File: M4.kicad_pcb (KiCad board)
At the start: 2 copper layers, 57.5 x 105 mm, 181 parts, among them J1 PJ-301B, J10 PJ-301B, J11 PJ-301B, J12 PJ-301B, J13 PJ-301B, J2 PJ-301B, J3 PJ-301B, J4 PJ-301B, J5 PJ-301B, J6 PJ-301B, J7 PJ-301B, J8 PJ-301B, J9 PJ-301B, P1 CONN_01X01, P2 CONN_01X01, P3 CONN_01X01, P4 CONN_01X01, P5 CONN_01X06, P6 CONN_02X05, P7 CONN_01X01, SW1 B3F-1050, SW2 B3F-1050, SW3 B3F-1050, SW4 B3F-1050, SW5 B3F-1050, SW6 B3F-1050, SW7 B3F-1050, U1 LM1117, U10 STM32F410RBTx, U2 MCP1703, U3 MAX5134, U4 74ACT541, U5 OPA4171, U6 OPA171, U7 OPA171, U8 CD4051, U9 OPA4171, X1 MIDI IN, Y1 8MHz

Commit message: routing.
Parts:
- C1, C10, C11, C33, C34, C4, C43, C44, C5, C6, C7, C8, C9, D24, D25, L1, L3, L4, P5, P6, R10, R11, R12, R13, R14, R15, R17, R18, R2, R20, R21, R8, R9, U6: moved to B.Cu
- Y1: footprint synth:HC-49-SM -> synth:403-XTAL-4-SMD
- moved L4 170.2 mm to (161.1, 55.0)
- moved L3 165.9 mm to (161.1, 39.5)
- moved D25 164.2 mm to (155.7, 52.1), turned to 270 degrees
- moved R14 162.3 mm to (134.2, 91.2), turned to 90 degrees
- moved C9 161.8 mm to (135.5, 88.5), turned to 180 degrees
- moved D24 161.3 mm to (155.7, 42.2), turned to 270 degrees
- moved U6 159.8 mm to (127.6, 96.2), turned to 270 degrees
- moved C33 158.3 mm to (134.5, 83.4)
- moved R8 157.6 mm to (131.4, 87.1), turned to 270 degrees
- moved R13 157.3 mm to (127.7, 91.9)
- moved R12 156.3 mm to (127.7, 90.1), turned to 180 degrees
- moved R17 156.2 mm to (136.0, 76.9)
- moved R9 156.1 mm to (129.6, 87.1), turned to 270 degrees
- moved R18 153.6 mm to (133.0, 76.9), turned to 180 degrees
- moved C8 152.6 mm to (130.6, 78.9), turned to 180 degrees
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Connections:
- U3 pad 11: Net-(U3-Pad11) -> /DAC_CH2
- U3 pad 14: Net-(U3-Pad14) -> /DAC_CH1
- U3 pad 3: Net-(U3-Pad3) -> /DAC_CH0
- U3 pad 6: Net-(U3-Pad6) -> /DAC_CH3
- U5 pad 10: Net-(U3-Pad11) -> /DAC_CH1
- U5 pad 12: Net-(U3-Pad6) -> /DAC_CH2
- U5 pad 3: Net-(U3-Pad3) -> /DAC_CH3
- U5 pad 5: Net-(U3-Pad14) -> /DAC_CH0
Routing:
- net Net-(C4-Pad1): track 0.00 -> 32.2 mm
- net /VREF: track 0.00 -> 26.8 mm
- net Net-(C8-Pad2): track 0.00 -> 21.7 mm
- net /DAC_CH1: track 0.00 -> 17.8 mm
- net /DAC_CH0: track 0.00 -> 17.7 mm
- net +3V3: track 0.00 -> 16.3 mm
- net /DAC_CH2: track 0.00 -> 14.2 mm
- net /DAC_CH3: track 0.00 -> 14.1 mm
- net Net-(C11-Pad2): track 0.00 -> 13.0 mm
- net /DAC_AVDD: track 0.00 -> 7.03 mm
- net Net-(R12-Pad1): track 0.00 -> 5.00 mm
- net +12V: track 0.00 -> 4.51 mm, vias 0 -> 2
- net Net-(C8-Pad1): track 0.00 -> 4.43 mm
- net Net-(C10-Pad2): track 0.00 -> 4.40 mm
- net -12V: track 0.00 -> 4.25 mm, vias 0 -> 2
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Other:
- board size 57.5 x 105 mm -> 57.2 x 105 mm
- net class Default: via_dia 0.6 -> 0.8
- net class POWER added: clearance 0.2, trace_width 0.4, via_dia 0.9, via_drill 0.45

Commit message: routing..
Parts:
- L2, P1, P2, R16, R22, R23, R24, R25, R26, R27, R28, R29, U7: moved to B.Cu
- moved U7 178.7 mm to (142.8, 116.8), turned to 270 degrees
- moved C12 159.1 mm to (110.0, 115.0)
- moved C13 159.1 mm to (110.0, 115.0)
- moved C16 159.1 mm to (110.0, 115.0)
- moved C17 159.1 mm to (110.0, 115.0)
- moved C18 159.1 mm to (110.0, 115.0)
- moved C19 159.1 mm to (110.0, 115.0)
- moved C20 159.1 mm to (110.0, 115.0)
- moved C21 159.1 mm to (110.0, 115.0)
- moved C22 159.1 mm to (110.0, 115.0)
- moved C23 159.1 mm to (110.0, 115.0)
- moved C24 159.1 mm to (110.0, 115.0)
- moved C25 159.1 mm to (110.0, 115.0)
- moved C26 159.1 mm to (110.0, 115.0)
- moved C27 159.1 mm to (110.0, 115.0)
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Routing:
- net /MIDI_RX: track 0.00 -> 117.6 mm, vias 0 -> 2
- net /12b_DAC: track 0.00 -> 101.9 mm, vias 0 -> 2
- net +3V3: track 16.3 -> 110.5 mm, vias 0 -> 3
- net +12V: track 4.51 -> 59.9 mm, vias 2 -> 3
- net -12V: track 4.25 -> 55.6 mm, vias 2 -> 3
- net Net-(C46-Pad1): track 0.00 -> 43.7 mm, vias 0 -> 1
- net /LED11: track 0.00 -> 33.3 mm, vias 0 -> 1
- net /~DAC_SEL: track 0.00 -> 33.2 mm, vias 0 -> 2
- net /LED3: track 0.00 -> 28.6 mm, vias 0 -> 1
- net /LED10: track 0.00 -> 26.7 mm, vias 0 -> 1
- net /DAC_SCK: track 0.00 -> 26.4 mm, vias 0 -> 2
- net /~LDAC: track 0.00 -> 25.6 mm, vias 0 -> 2
- net /SWCLK: track 0.00 -> 25.4 mm, vias 0 -> 2
- net Net-(C45-Pad1): track 0.00 -> 23.5 mm, vias 0 -> 1
- net /LED2: track 0.00 -> 23.1 mm, vias 0 -> 1
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
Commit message: routing...
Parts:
- C12, C17, C26, C27, C28, C29, C30, C31, C45, D22, P7, R30, R31, R32, R33, R34, R41, R47, R52, R53: moved to B.Cu
- moved P7 73.9 mm to (126.5, 43.0)
- moved C45 71.7 mm to (133.5, 47.3), turned to 180 degrees
- moved C27 70.7 mm to (130.4, 47.3)
- moved C29 68.0 mm to (112.3, 47.0), turned to 180 degrees
- moved C17 66.6 mm to (129.8, 51.4)
- moved R53 65.9 mm to (112.3, 49.1), turned to 180 degrees
- moved C30 65.0 mm to (129.8, 53.1)
- moved C28 63.3 mm to (129.8, 54.9)
- moved R32 60.8 mm to (145.1, 65.4), turned to 180 degrees
- moved R33 60.7 mm to (142.6, 63.8), turned to 90 degrees
- moved C31 56.2 mm to (117.1, 59.2), turned to 270 degrees
- moved C26 56.1 mm to (115.3, 59.2), turned to 270 degrees
- moved R31 55.7 mm to (135.9, 65.7), turned to 180 degrees
- moved R30 52.9 mm to (126.8, 64.8), turned to 90 degrees
- moved R34 48.1 mm to (155.4, 130.8), turned to 90 degrees
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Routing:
- net /MODE_SW: track 0.00 -> 133.0 mm, vias 0 -> 1
- net /CH3_SW: track 0.00 -> 109.4 mm, vias 0 -> 1
- net /MIDI_LED: track 0.00 -> 104.3 mm, vias 0 -> 3
- net /LED12: track 0.00 -> 81.0 mm, vias 0 -> 1
- net /GATE4_LED: track 0.00 -> 71.5 mm, vias 0 -> 2
- net /D1: track 0.00 -> 60.9 mm, vias 0 -> 1
- net /D0: track 0.00 -> 59.9 mm, vias 0 -> 1
- net /GATE_3: track 0.00 -> 59.2 mm, vias 0 -> 1
- net /CLOCK: track 0.00 -> 57.3 mm, vias 0 -> 1
- net /GATE3_LED: track 0.00 -> 57.1 mm, vias 0 -> 2
- net /~MUX_SEL: track 0.00 -> 56.8 mm, vias 0 -> 1
- net /REC_SW: track 9.47 -> 63.5 mm, vias 1 -> 2
- net +3V3: track 110.5 -> 154.5 mm, vias 3 -> 5
- net /GATE2_LED: track 0.00 -> 41.6 mm, vias 0 -> 2
- net /GATE1_LED: track 8.07 -> 29.4 mm, vias 1 -> 2
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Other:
- net class Default: trace_width 0.25 -> 0.2; via_dia 0.8 -> 0.7; via_drill 0.4 -> 0.35

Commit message: routing....
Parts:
- C47, D23, R4, R62, R63: moved to B.Cu
- moved R63 30.5 mm to (137.7, 127.8), turned to 270 degrees
- moved C47 30.3 mm to (133.7, 133.9)
- moved R4 26.4 mm to (135.2, 122.8), turned to 180 degrees
- moved R62 19.2 mm to (120.0, 131.4), turned to 180 degrees
- moved D23 17.4 mm to (120.9, 128.6), turned to 270 degrees
- moved R22 5.61 mm to (138.0, 50.1)
- moved R24 4.53 mm to (138.6, 53.1), turned to 270 degrees
- moved C2 3.91 mm to (113.9, 113.9)
- moved C13 3.91 mm to (113.8, 114.1)
- moved C16 3.91 mm to (113.8, 114.1)
- moved C18 3.91 mm to (113.8, 114.1)
- moved C19 3.91 mm to (113.8, 114.1)
- moved C20 3.91 mm to (113.8, 114.1)
- moved C21 3.91 mm to (113.8, 114.1)
- moved C22 3.91 mm to (113.8, 114.1)
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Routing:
- net /LED13: track 2.83 -> 138.1 mm, vias 1 -> 2
- net /LED15: track 2.97 -> 137.9 mm, vias 1 -> 2
- net /LED14: track 2.79 -> 136.2 mm, vias 1 -> 2
- net /CH4_SW: track 2.24 -> 119.2 mm
- net +3V3: track 154.5 -> 262.6 mm, vias 5 -> 7
- net /CH2_SW: track 2.27 -> 93.6 mm
- net /GATE_2: track 2.04 -> 78.9 mm, vias 1 -> 2
- net /GATE_1: track 2.27 -> 78.1 mm, vias 1 -> 2
- net /CH1_SW: track 2.45 -> 77.8 mm
- net +12V: track 74.1 -> 147.9 mm
- net /GATE_4: track 1.69 -> 70.5 mm, vias 1 -> 2
- net -12V: track 66.9 -> 129.7 mm, vias 4 -> 6
- net +5V: track 0.00 -> 48.3 mm
- net /LED12: track 81.0 -> 127.6 mm, vias 1 -> 2
- net Net-(D23-Pad2): track 0.00 -> 19.8 mm
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
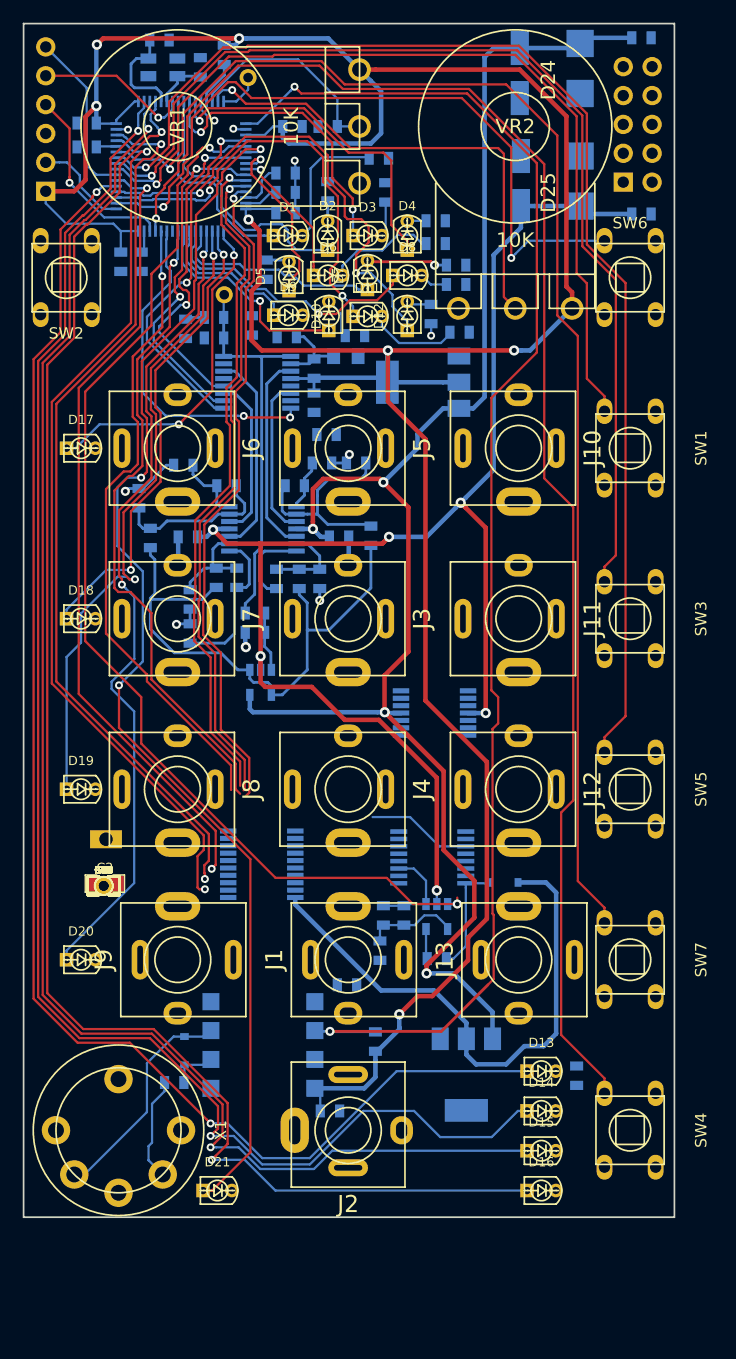
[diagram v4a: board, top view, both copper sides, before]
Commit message: basically routed. need to delete excess decoupling caps and decide about whether external sw pull up resistors are necessary - probably not and need to be deleted
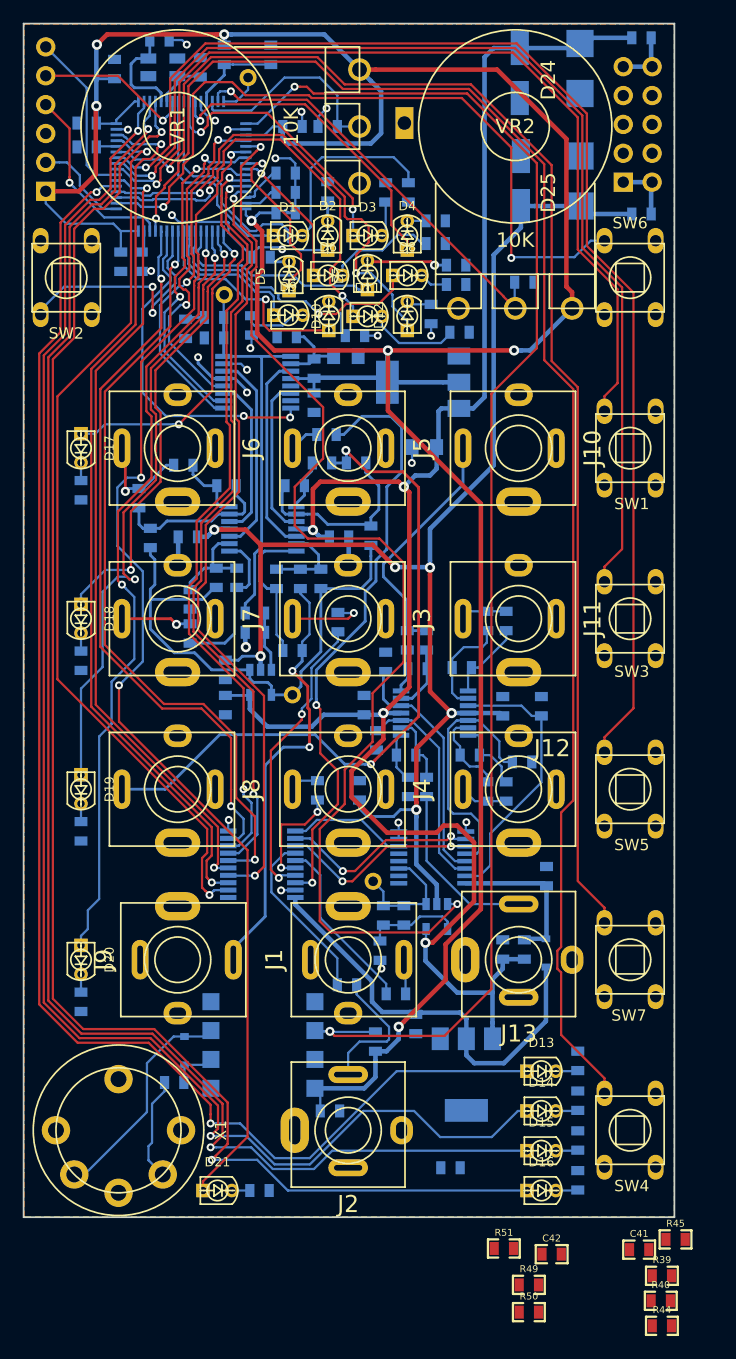
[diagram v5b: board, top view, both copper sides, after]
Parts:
- C13, C16, C18, C19, C2, C20, C21, C22, C23, C24, C25, C3, C32, C35, C36, C37, C38, C39, C40, C46, P3, P4, R1, R19, R3, R35, R36, R37, R38, R42, R43, R46, R48, R5, R54, R55, R56, R57, R58, R59, R6, R60, R61: moved to B.Cu
- moved C32 74.6 mm to (128.5, 41.0), turned to 90 degrees
- moved C16 71.9 mm to (114.8, 42.2), turned to 90 degrees
- moved P1 68.2 mm to (140.2, 47.0), turned to 90 degrees
- moved C46 64.7 mm to (150.8, 61.0)
- moved R44 62.5 mm to (162.9, 152.8)
- moved R40 61.1 mm to (162.8, 150.6)
- moved R39 59.9 mm to (162.9, 148.4)
- moved R45 59.1 mm to (164.1, 145.2)
- moved C41 56.9 mm to (160.9, 146.1)
- moved R50 53.0 mm to (151.2, 151.6)
- moved R49 51.3 mm to (151.2, 149.2)
- moved C42 51.0 mm to (153.2, 146.5)
- moved R37 49.1 mm to (155.5, 140.0), turned to 270 degrees
- moved C2 47.6 mm to (142.0, 75.5), turned to 180 degrees
- moved R51 47.5 mm to (149.0, 146.0)
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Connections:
- R14 pad 1: Net-(J7-Pad3) -> Net-(J9-Pad3)
- R15 pad 1: Net-(J8-Pad3) -> Net-(J7-Pad3)
- R16 pad 1: Net-(J9-Pad3) -> Net-(J6-Pad3)
- R17 pad 1: Net-(J6-Pad3) -> Net-(J8-Pad3)
- R18 pad 1: Net-(J6-Pad3) -> Net-(J8-Pad3)
- R19 pad 1: Net-(J7-Pad3) -> Net-(J9-Pad3)
- R20 pad 1: Net-(J8-Pad3) -> Net-(J7-Pad3)
- R21 pad 1: Net-(J9-Pad3) -> Net-(J6-Pad3)
- R55 pad 1: Net-(J11-Pad3) -> Net-(J13-Pad3)
- R56 pad 1: Net-(J12-Pad3) -> Net-(J11-Pad3)
- R57 pad 1: Net-(J13-Pad3) -> Net-(J12-Pad3)
- R59 pad 1: Net-(J11-Pad3) -> Net-(J13-Pad3)
- R60 pad 1: Net-(J12-Pad3) -> Net-(J11-Pad3)
- R61 pad 1: Net-(J13-Pad3) -> Net-(J12-Pad3)
- U9 pad 1: Net-(C22-Pad1) -> Net-(C23-Pad1)
- U9 pad 2: Net-(C22-Pad2) -> Net-(C23-Pad2)
- U9 pad 3: Net-(C18-Pad1) -> Net-(C19-Pad1)
- U9 pad 5: Net-(C19-Pad1) -> Net-(C18-Pad1)
- U9 pad 6: Net-(C23-Pad2) -> Net-(C22-Pad2)
- U9 pad 7: Net-(C23-Pad1) -> Net-(C22-Pad1)
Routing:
- net Net-(J8-Pad3): track 2.52 -> 61.2 mm, vias 1 -> 2
- net Net-(R7-Pad2): track 0.00 -> 53.2 mm, vias 0 -> 2
- net GND: track 16.5 -> 55.1 mm, vias 6 -> 23
- net Net-(J9-Pad3): track 5.20 -> 38.3 mm, vias 1 -> 2
- net Net-(R5-Pad2): track 0.00 -> 25.9 mm, vias 0 -> 2
- net Net-(C20-Pad1): track 0.00 -> 24.4 mm
- net Net-(C21-Pad1): track 0.00 -> 22.4 mm
- net /PARAM_SW: track 0.00 -> 21.9 mm, vias 0 -> 2
- net Net-(J10-Pad3): track 0.00 -> 21.5 mm
- net Net-(C18-Pad1): track 0.00 -> 21.4 mm
- net Net-(C19-Pad1): track 0.00 -> 19.0 mm
- net /B: track 0.00 -> 17.6 mm, vias 0 -> 2
- net Net-(J13-Pad3): track 0.00 -> 16.9 mm
- net +12V: track 147.9 -> 163.5 mm
- net Net-(R3-Pad2): track 0.00 -> 15.6 mm
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- added copper zone on B.Cu, net GND
- added copper zone on F.Cu, net GND

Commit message: routed.
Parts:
- C41, C42, R39, R40, R44, R45, R49, R50, R51: moved to B.Cu
- moved R40 105.4 mm to (109.1, 59.9), turned to 180 degrees
- moved C41 99.8 mm to (145.4, 47.5), turned to 180 degrees
- moved R50 90.4 mm to (158.7, 61.5), turned to 180 degrees
- moved C42 89.2 mm to (160.1, 57.6), turned to 90 degrees
- moved R39 78.7 mm to (158.7, 69.8), turned to 180 degrees
- moved R44 63.1 mm to (158.7, 89.8), turned to 180 degrees
- moved R49 43.4 mm to (158.7, 106.5), turned to 180 degrees
- moved R51 26.4 mm to (158.7, 121.5), turned to 180 degrees
- moved R45 10.3 mm to (158.7, 136.4), turned to 180 degrees
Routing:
- net +3V3: track 260.9 -> 346.8 mm
- net GND: track 55.1 -> 69.2 mm, vias 23 -> 26
- net +12V: track 163.5 -> 160.5 mm
- net /CH1_SW: track 80.2 -> 82.7 mm
- net /PARAM_SW: track 21.9 -> 24.4 mm
- net /CH2_SW: track 95.4 -> 97.8 mm
- net /MODE_SW: track 135.0 -> 137.4 mm
- net /REC_SW: track 64.7 -> 67.0 mm
- net /CH3_SW: track 111.2 -> 113.6 mm
- net /CH4_SW: track 119.2 -> 121.6 mm
- net -12V: track 126.2 -> 128.0 mm

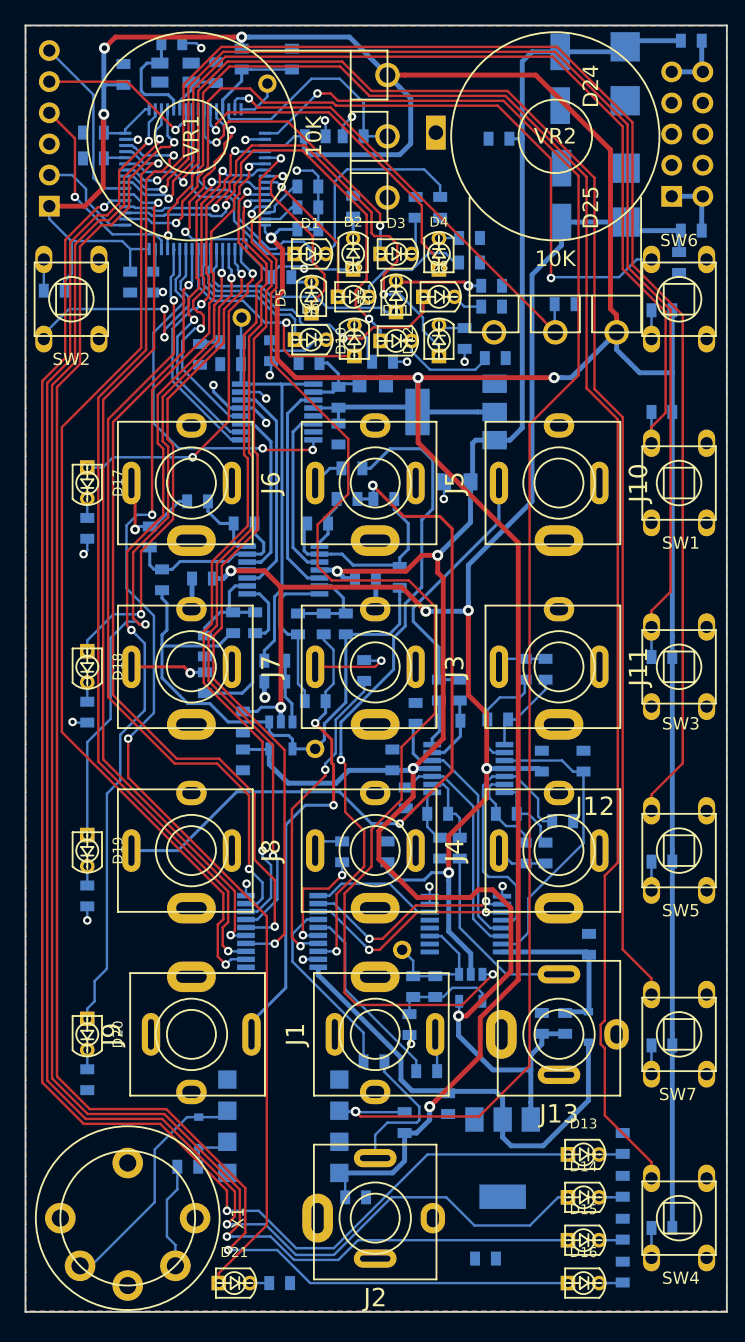
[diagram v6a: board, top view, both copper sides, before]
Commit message: updated some 3D part assignments
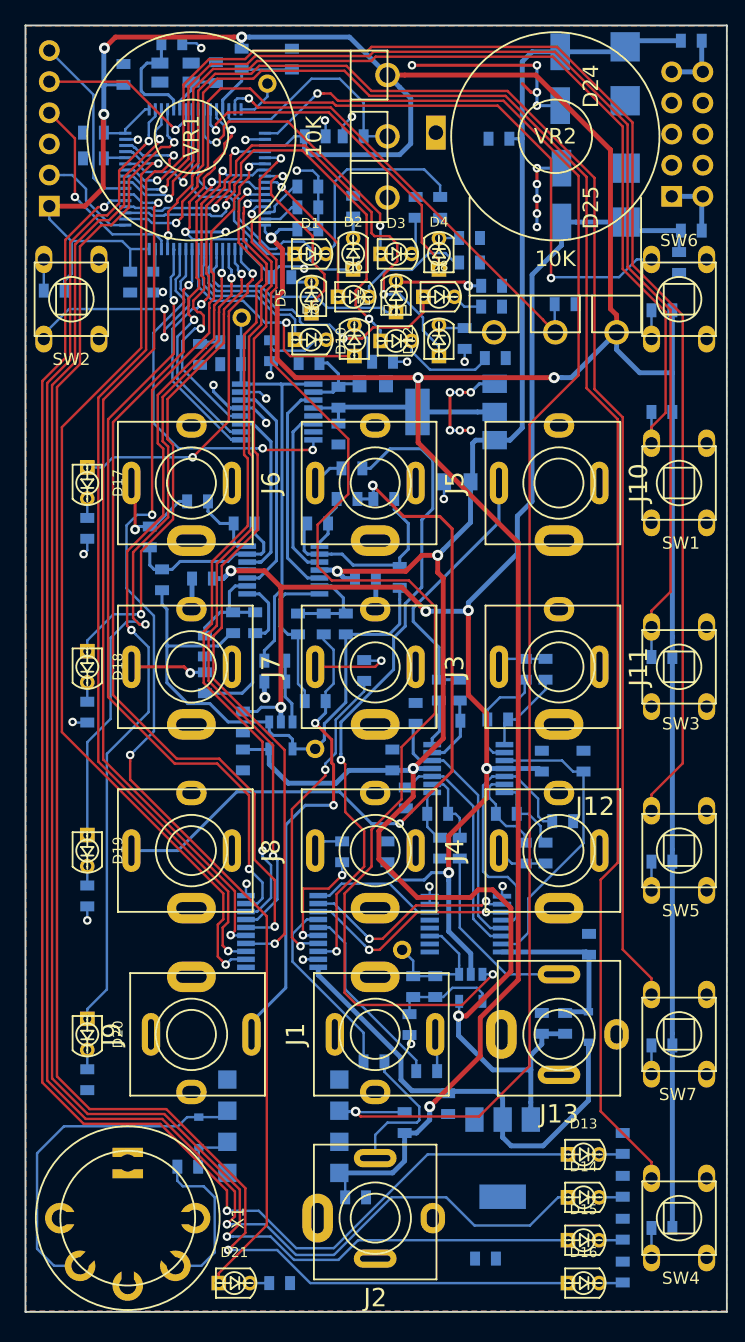
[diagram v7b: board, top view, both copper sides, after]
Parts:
- X1: footprint MyModules:SD-50BV-5DIN -> MyModules:SD-50BV-5DIN-SLOTS
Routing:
- net GND: track 69.2 -> 104.9 mm, vias 26 -> 42
- net Net-(D23-Pad2): track 19.8 -> 28.8 mm
- net Net-(R62-Pad2): track 8.73 -> 12.0 mm
- net /VREF: track 47.7 -> 46.9 mm
